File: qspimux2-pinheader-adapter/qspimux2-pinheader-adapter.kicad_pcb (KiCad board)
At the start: 2 copper layers, 22.3 x 14 mm, 5 parts, among them J1 Conn_01x10_MountingPin, J2 Conn_02x05_Odd_Even

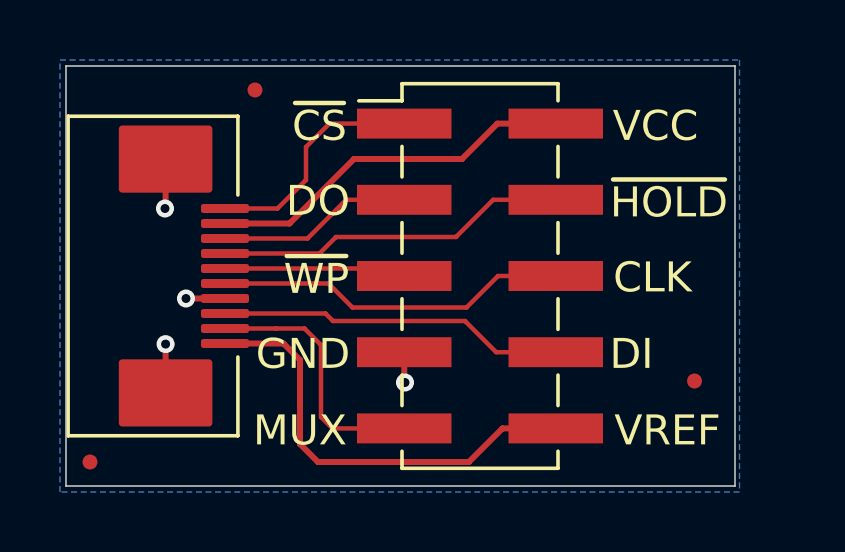
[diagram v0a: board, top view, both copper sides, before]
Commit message: improve qspimux2 manufacturability
move the vias to the ground planes a bit away from the components
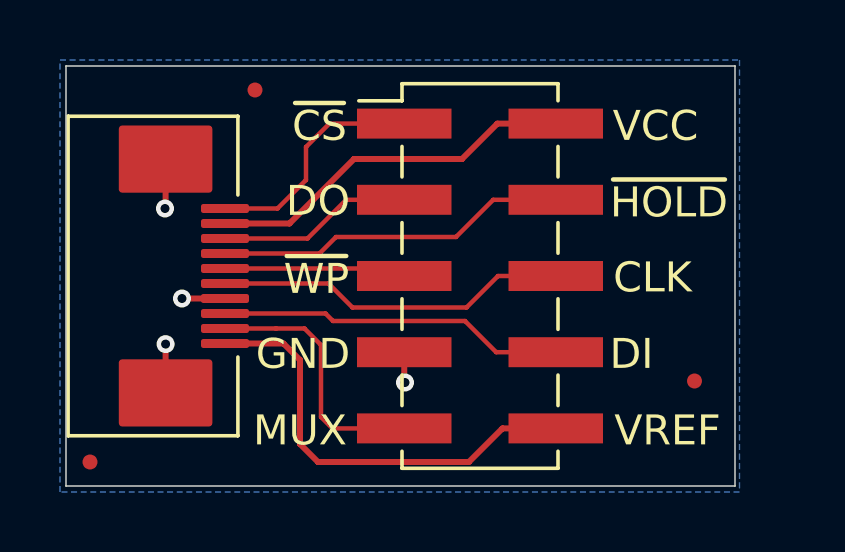
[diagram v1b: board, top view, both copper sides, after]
